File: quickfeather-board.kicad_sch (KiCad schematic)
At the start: 101 parts, among them IC1 EOS-S3-QFN, J1 61300211121, J2 1x12_pinhead, J3 1x16_pinhead, J4 S2B-PH-SM4-TB_LF__SN_, J5 0473460001, J6 FTSH-105-01-L-DV-K, J7 61300211121, J8 2x8_pinhead, M1 mounting_pad, M2 mounting_pad, M3 mounting_pad, M4 mounting_pad, Q1 NX3008CBKV, Q2 2N7002PV, Q3 2N7002PV, Q4 DMG1012T-7, U1 TPS62821DLCR, U2 MCP73831T-2ACI_OT, U3 GD25Q16CWIGR, U4 DPS310, U5 MC3635, X1 ECS-_327-12_5-34B-TR

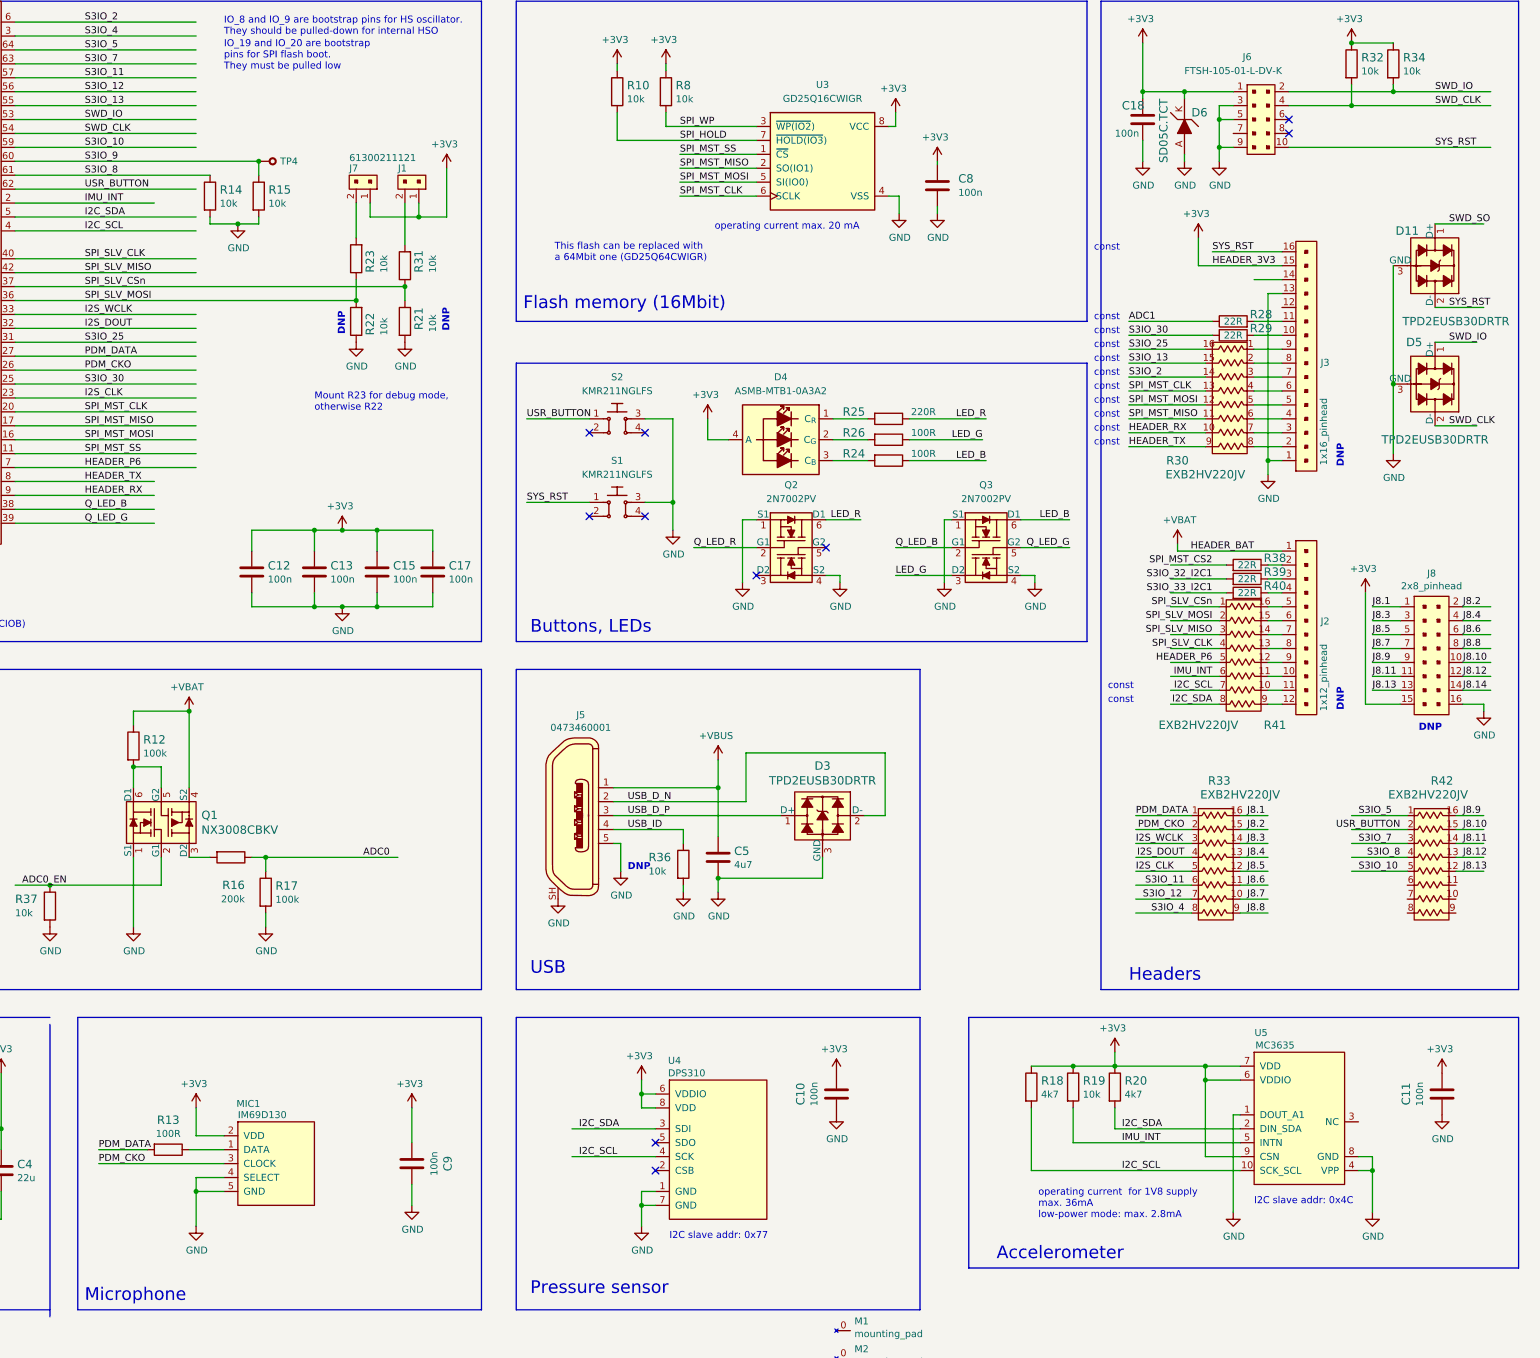
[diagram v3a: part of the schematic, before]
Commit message: [#54927] Standardize Microphone and USB connectors
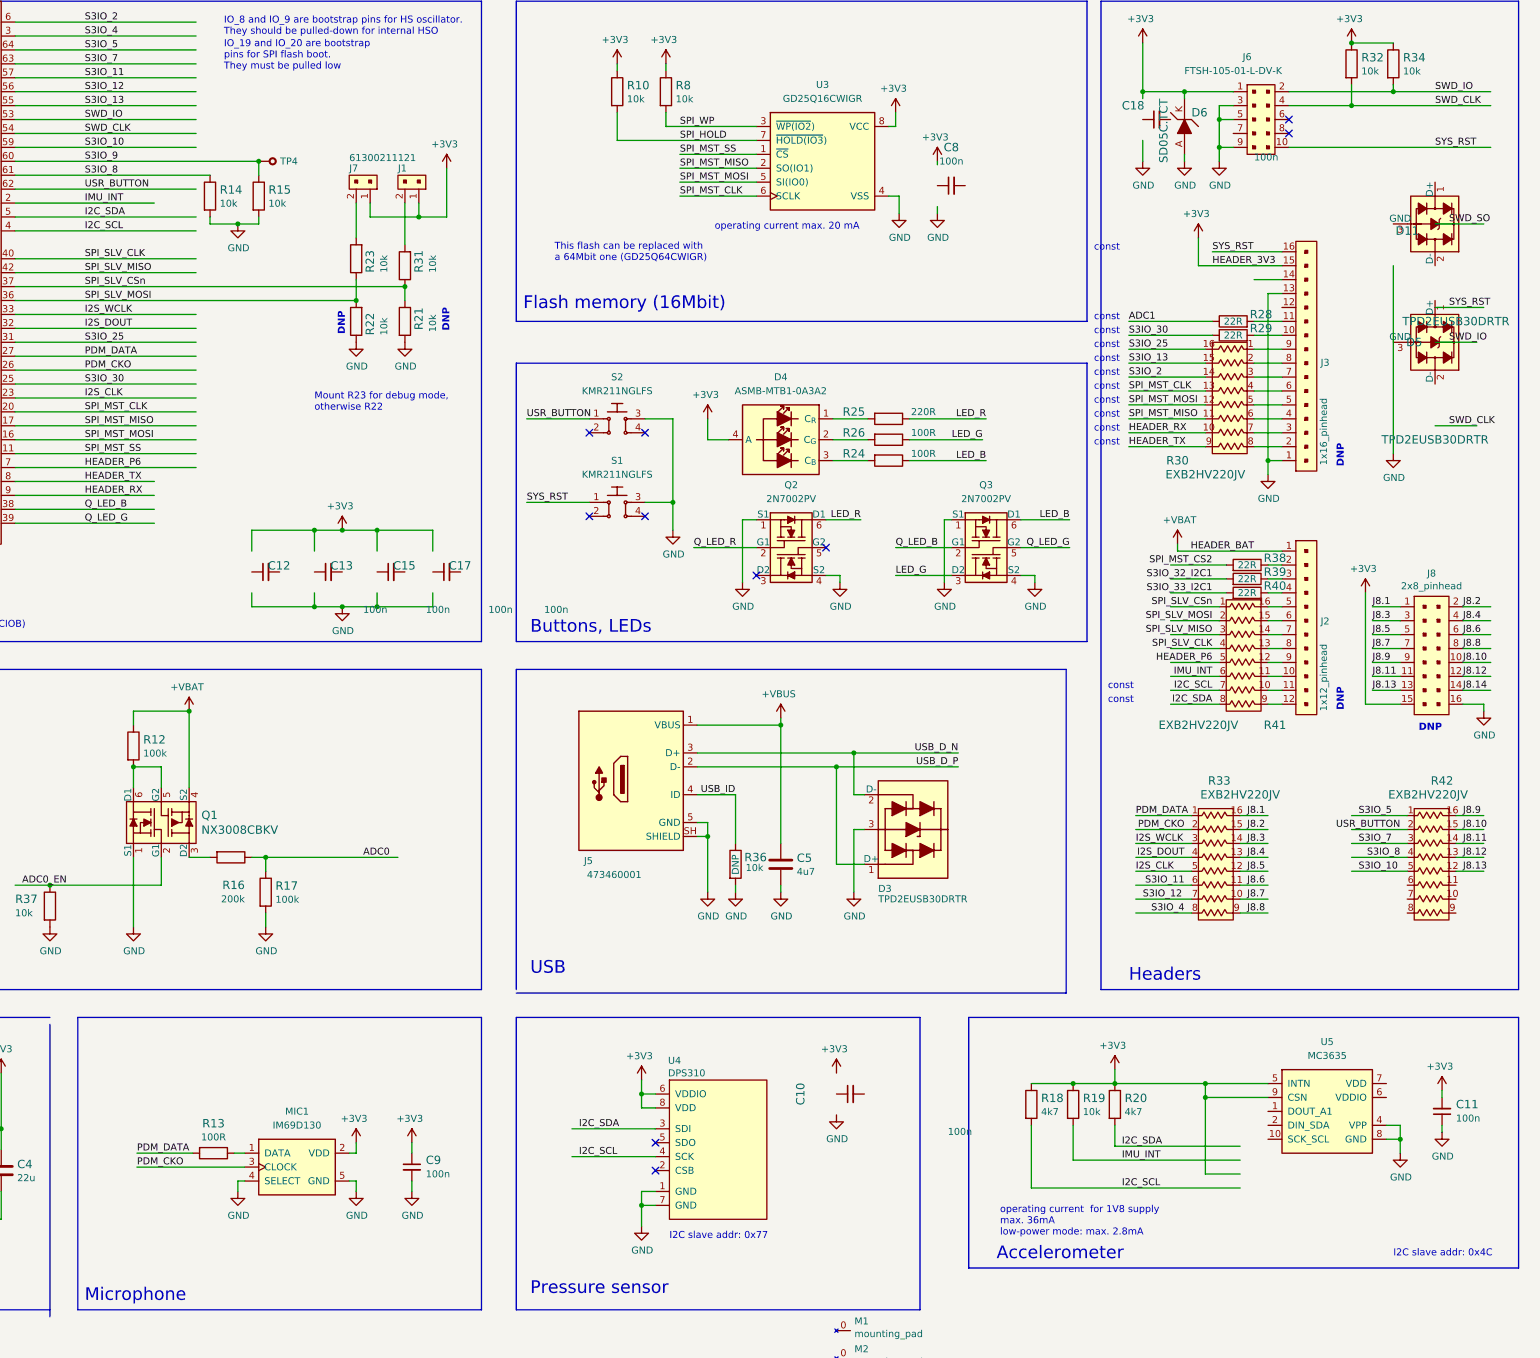
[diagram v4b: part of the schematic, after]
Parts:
- C10, C11, C12, C13, C15, C17, C18, C8, C9: value C_100n_0402_6V3 -> C_100n_0402; footprint quickfeather-board-footprints:0402-cap -> antmicro-footprints:C_0402_1005Metric; symbol quickfeather-board:C_100n_0402_6V3 -> antmicroCapacitors0402:C_100n_0402; Author (none) -> Antmicro; Dielectric (none) -> X5R; License (none) -> Apache-2.0; MPN 0402X104K6R3CT -> GRM155R61H104KE14D; Manufacturer Walsin -> Murata; Voltage (none) -> 50V
- D11, D3, D5, MIC1, U5: Author (none) -> Antmicro; License (none) -> Apache-2.0
- J5: footprint quickfeather-board-footprints:USB_Micro_B_Female_0473460001 -> antmicro-footprints:USB-Micro-B_Receptacle_Molex_473460001; symbol quickfeather-board:0473460001 -> antmicroUSBConnectors:USB-Micro-B_Molex_473460001; Author (none) -> Antmicro; License (none) -> Apache-2.0; MPN 0473460001 -> 473460001
- R36: DNP 1 -> DNP
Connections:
- net +3V3: now also C11.2, C9.1, U5.5 (INTN); no longer C10.1, C11.1, C12.1, C13.1, C15.1, C17.1, C18.1, C8.1, C9.2, U5.6 (VDDIO), U5.7 (VDD)
- net GND: now also C11.1, C9.2; no longer C10.2, C11.2, C12.2, C13.2, C15.2, C17.2, C18.2, C8.2, C9.1, D11.3 (GND), D5.3 (GND), U5.1 (DOUT_A1)
- net I2C_SCL: no longer U5.10 (SCK_SCL)
- net I2C_SDA: no longer U5.2 (DIN_SDA)
- net IMU_INT: no longer U5.5 (INTN)
- net SWD_CLK: no longer D5.2 (D-)
- net SWD_IO: no longer D5.1 (D+)
- net SWD_SO: no longer D11.1 (D+)
- net SYS_RST: no longer D11.2 (D-)
- net USB_D_N: now also J5.3 (D+); no longer J5.2
- net USB_D_P: now also J5.2 (D-); no longer J5.3
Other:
- moved on the sheet: C10, C11, C12, C13, C15, C17, C18, C8, C9, D11, D5, R13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

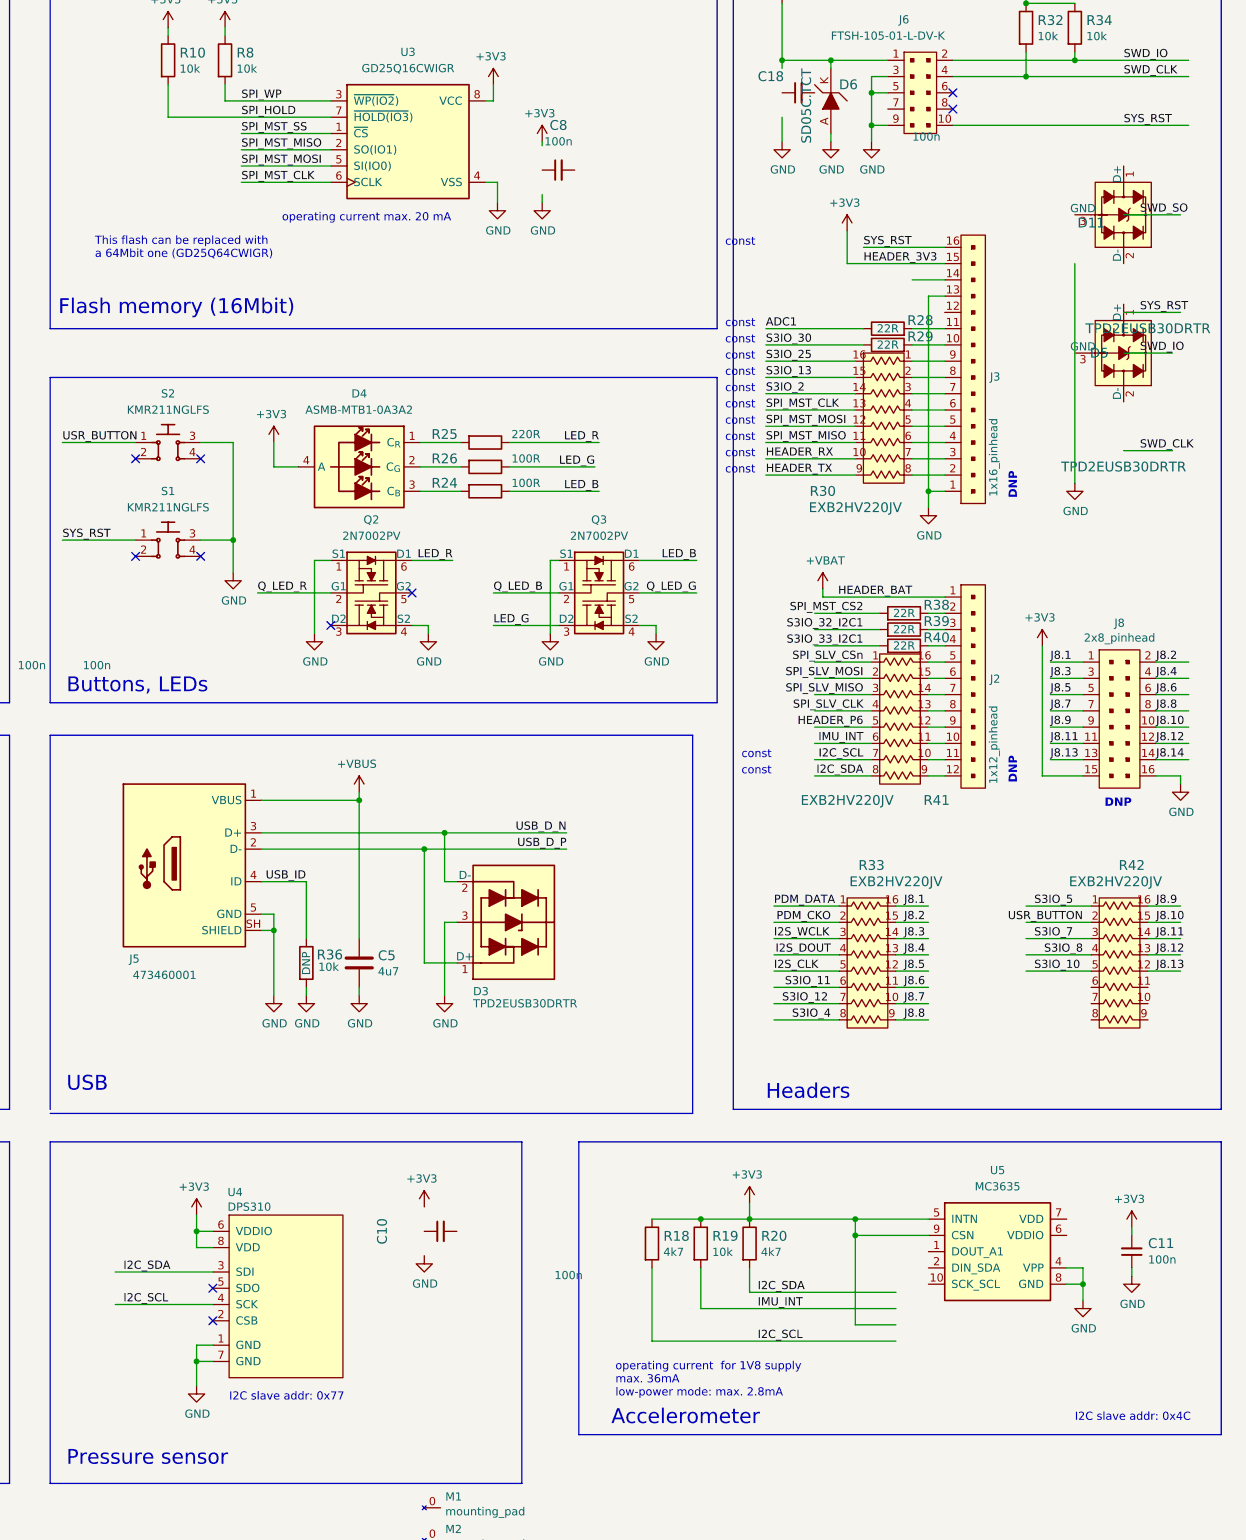
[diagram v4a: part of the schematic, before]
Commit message: [#54927] Standardize Accelerometer and pressure sensor
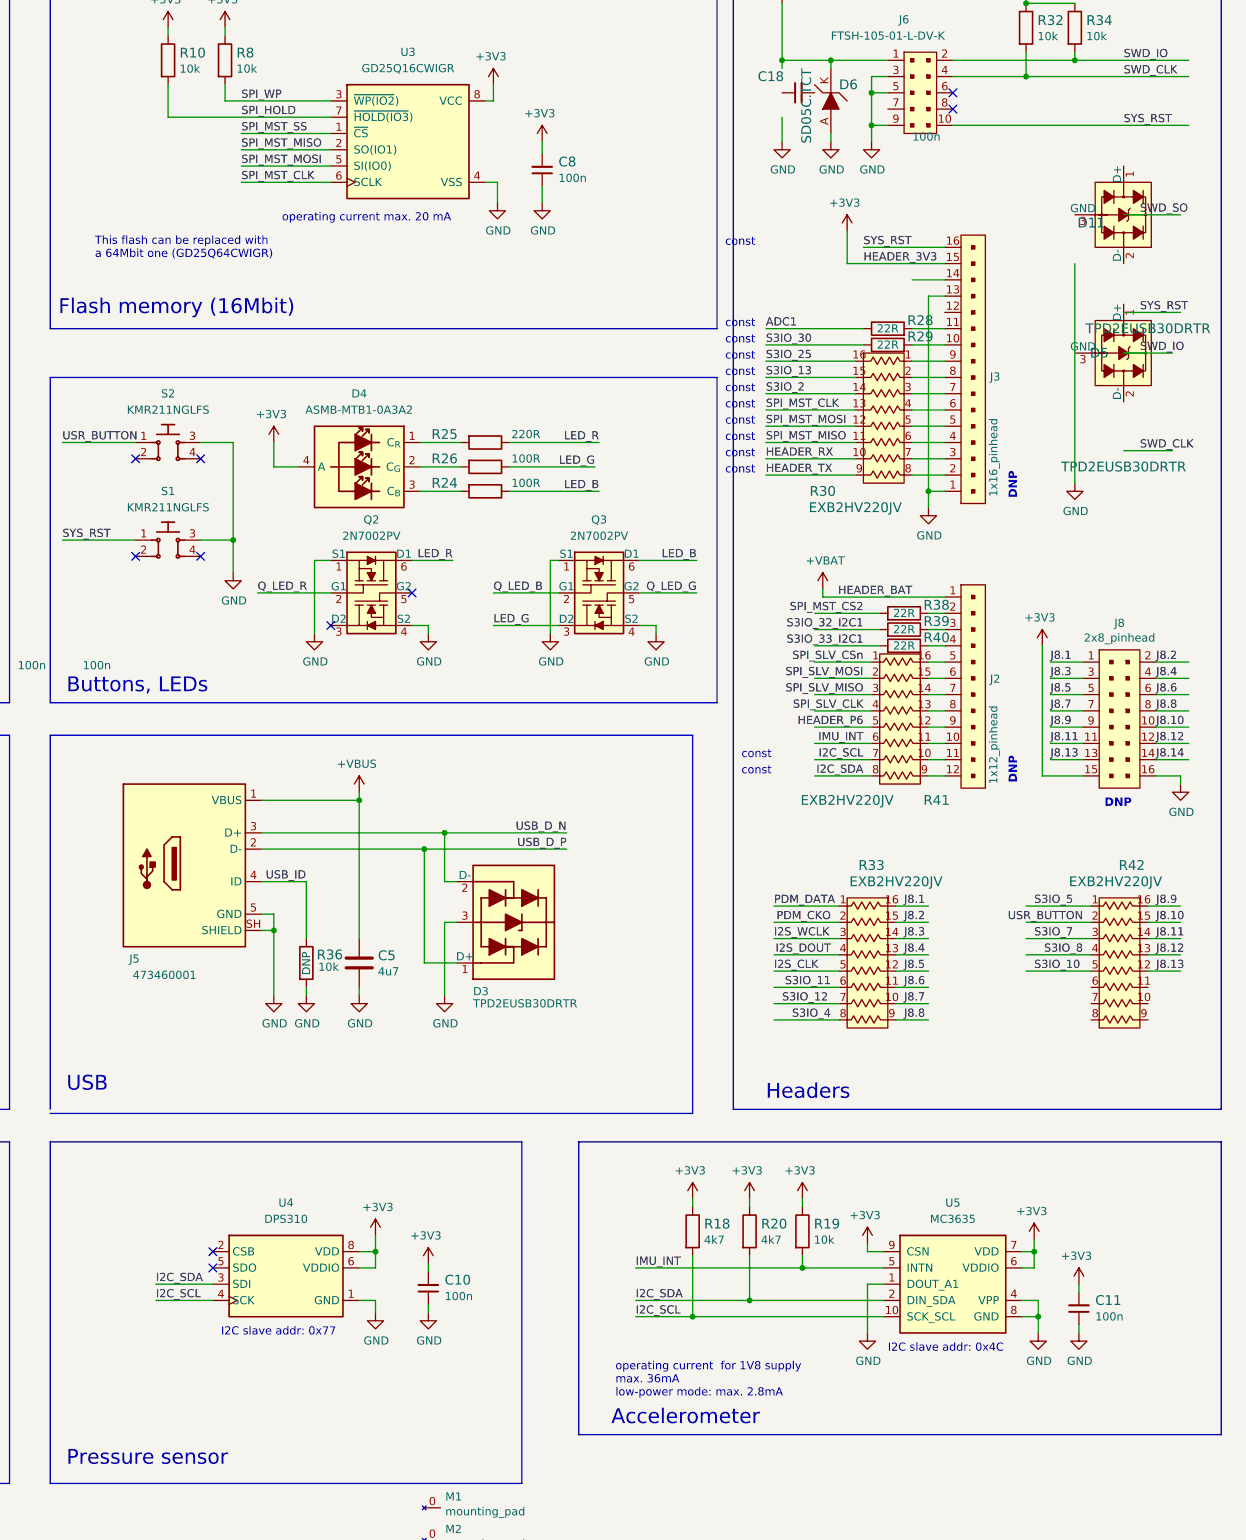
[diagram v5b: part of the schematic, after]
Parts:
- U4: footprint quickfeather-board-footprints:PG-VLGA-8-2 -> antmicro-footprints:PG-VLGA-8-2; symbol quickfeather-board:DPS310 -> antmicroHumidityMoistureSensors:DPS310; Author (none) -> Antmicro; License (none) -> Apache-2.0
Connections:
- net +3V3: now also C10.2, C8.2, U5.6 (VDDIO), U5.7 (VDD); no longer U5.5 (INTN)
- net GND: now also C10.1, C8.1, U5.1 (DOUT_A1)
- net I2C_SCL: now also U5.10 (SCK_SCL)
- net I2C_SDA: now also U5.2 (DIN_SDA)
- net IMU_INT: now also U5.5 (INTN)
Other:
- moved on the sheet: C10, C11, C8, R18, R19, R20, U5
